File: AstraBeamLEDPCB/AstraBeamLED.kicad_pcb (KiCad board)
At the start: 2 copper layers, 75 x 55 mm, 21 parts

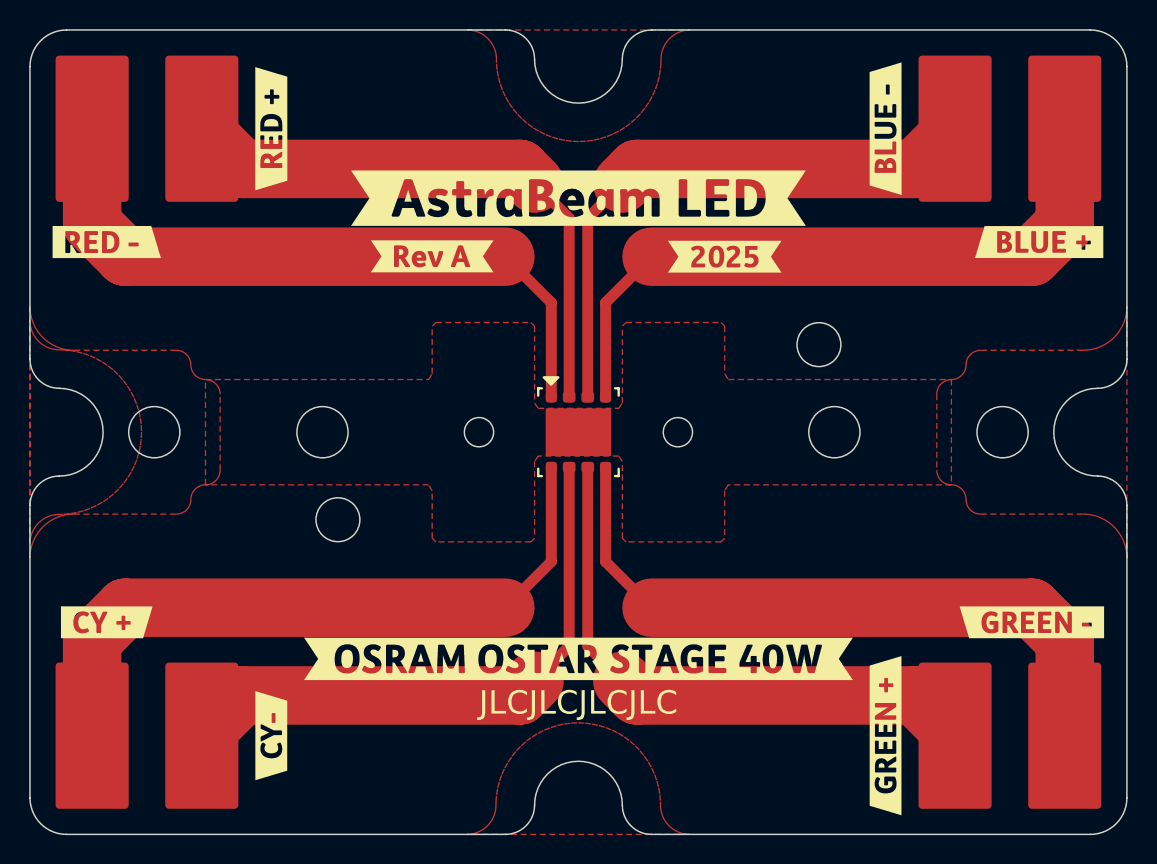
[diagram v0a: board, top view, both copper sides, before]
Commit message: Cleanup copper for production
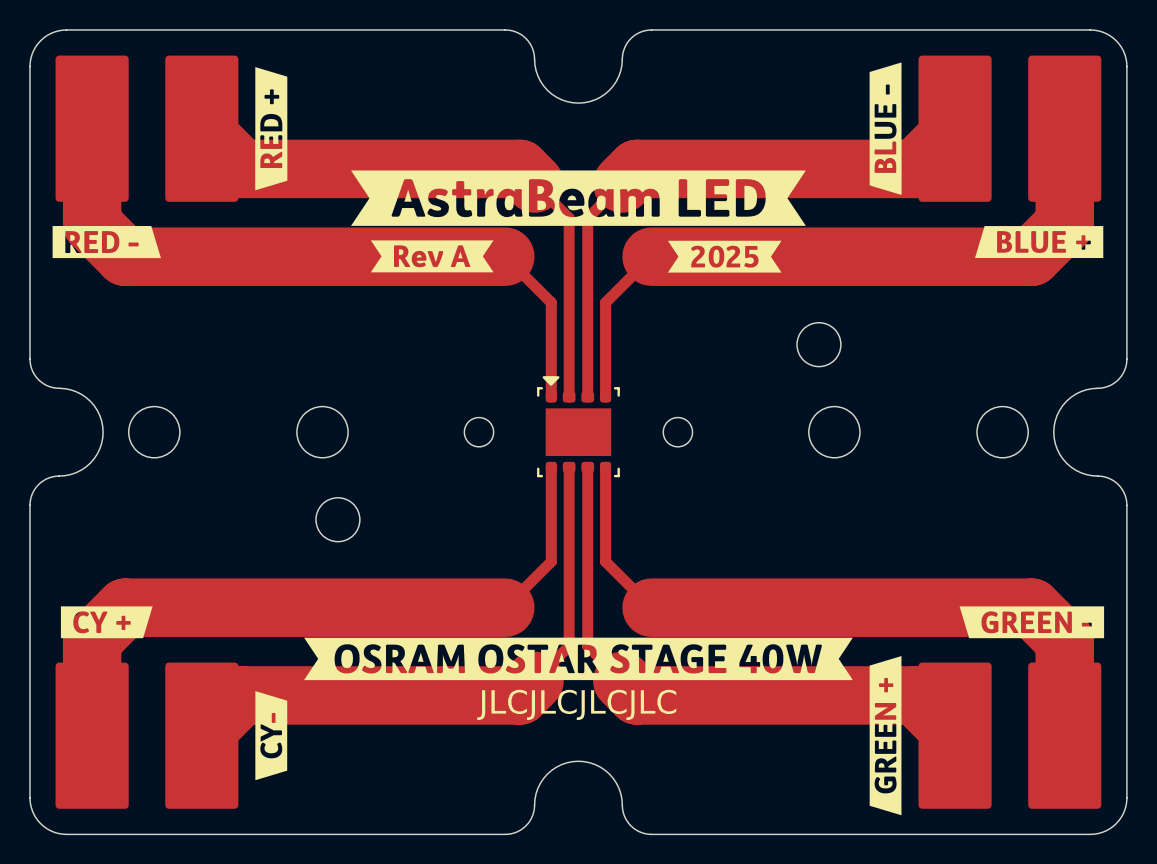
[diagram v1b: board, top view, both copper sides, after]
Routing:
- removed copper zone on F.Cu, net (none)
- removed copper zone on F.Cu, net GND

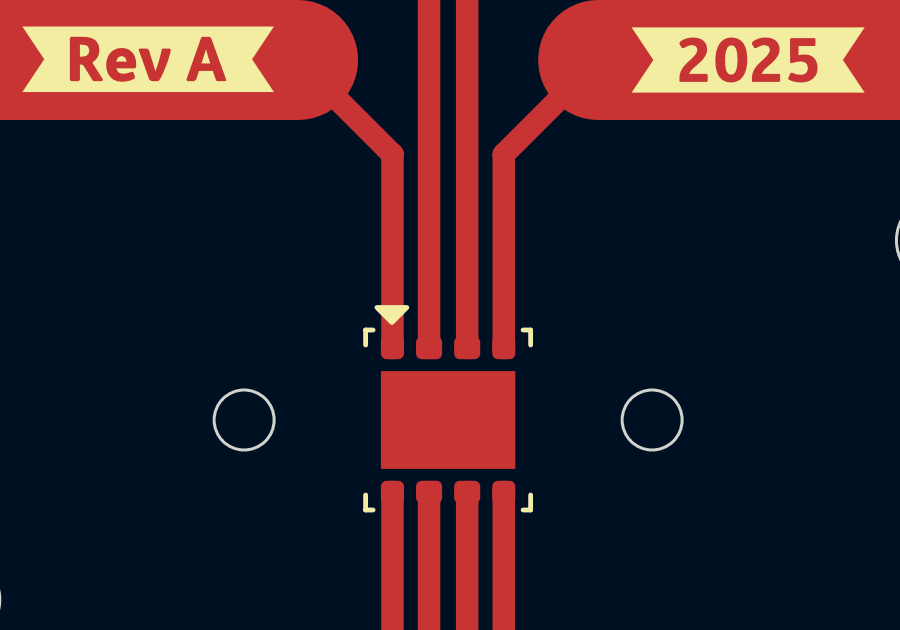
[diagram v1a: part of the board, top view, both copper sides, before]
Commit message: Fix reversed pins
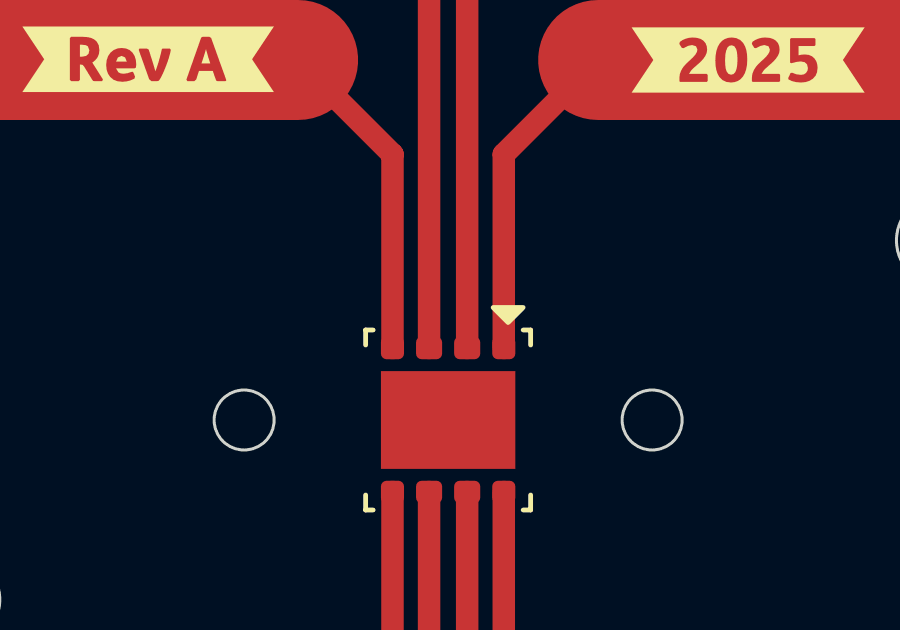
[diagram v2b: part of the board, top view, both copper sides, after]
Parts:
- moved J2 66.5 mm to (116.8, 79.2)
- moved J4 66.5 mm to (183.2, 120.8)
- moved J5 66.5 mm to (183.2, 79.2)
- moved J7 66.5 mm to (116.8, 120.8)
- moved J1 51.5 mm to (175.8, 79.2)
- moved J3 51.5 mm to (124.2, 120.8)
- moved J6 51.5 mm to (124.2, 79.2)
- moved J8 51.5 mm to (175.8, 120.8)

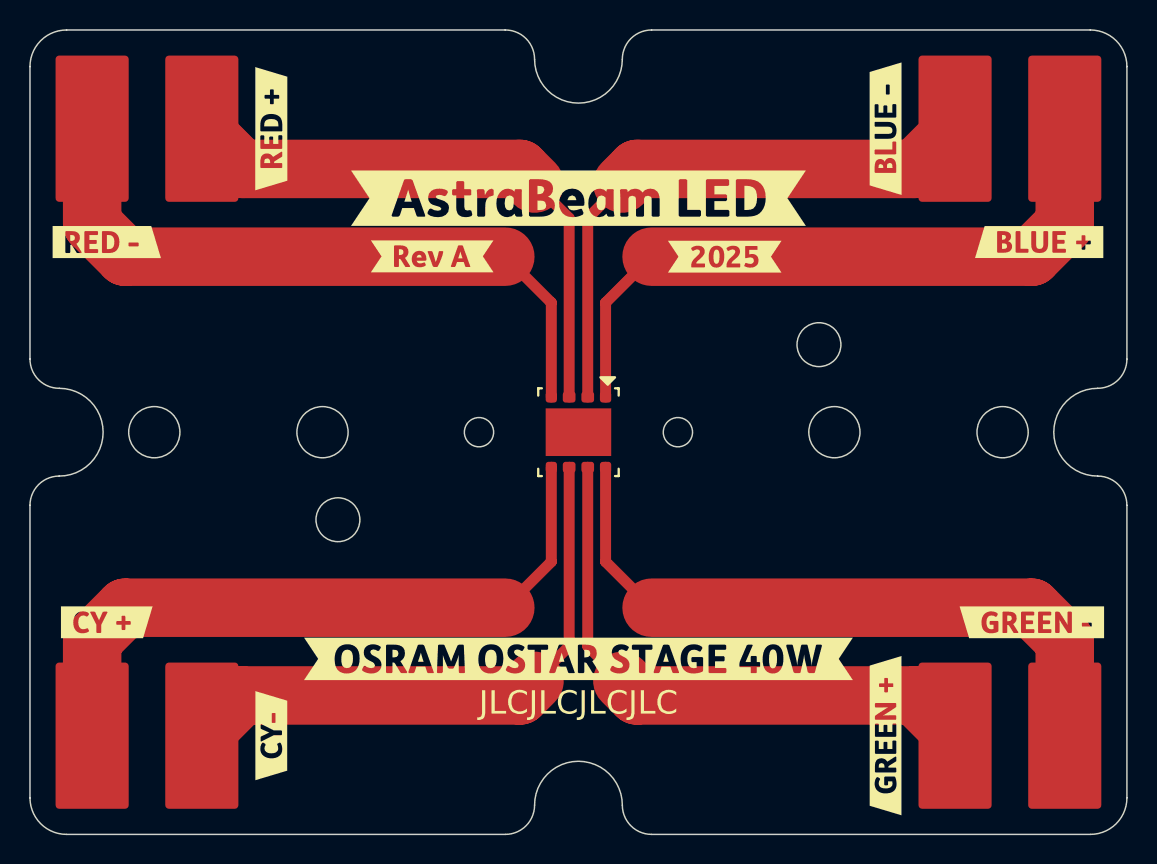
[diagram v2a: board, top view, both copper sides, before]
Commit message: Updated labels, description
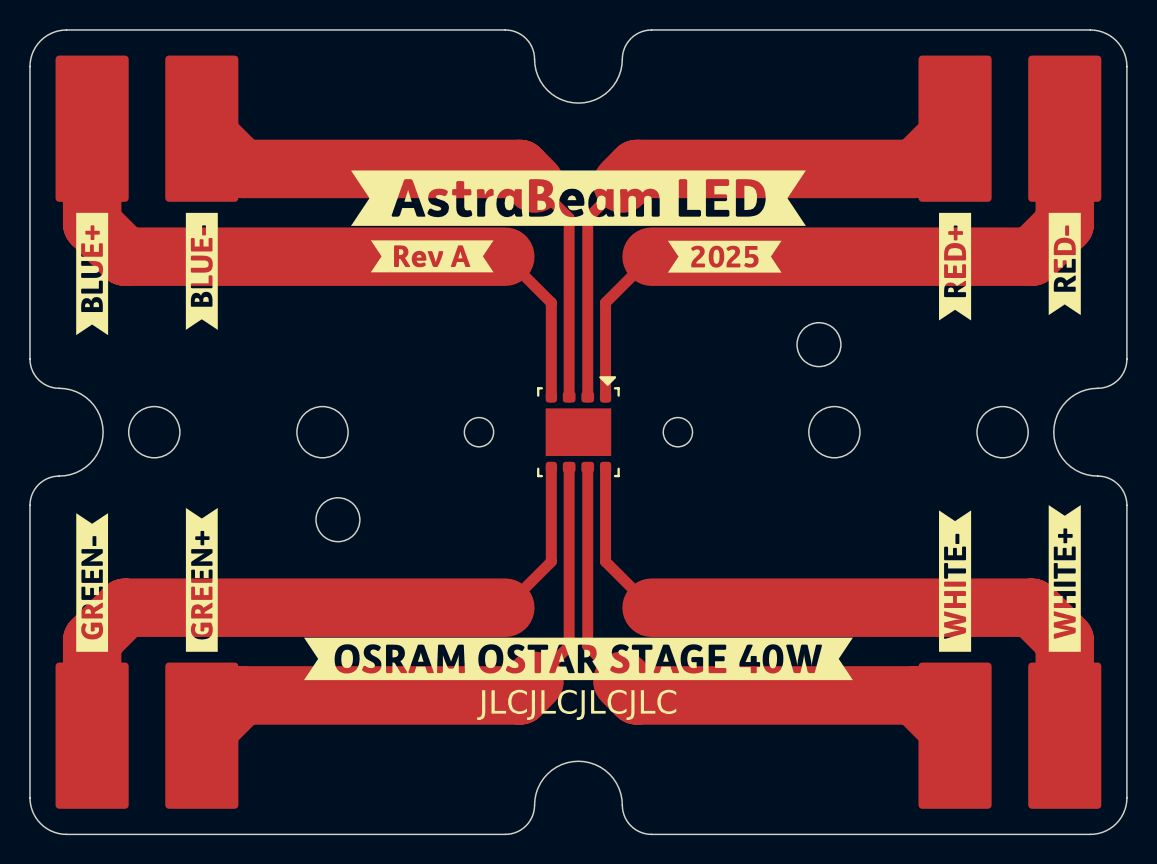
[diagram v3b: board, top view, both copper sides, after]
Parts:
- removed kibuzzard-67294C33: G***, kibuzzard-67294C33
- removed kibuzzard-67294C7C: G***, kibuzzard-67294C7C
- removed kibuzzard-67294CC4: G***, kibuzzard-67294CC4
- removed kibuzzard-67294E62: G***, kibuzzard-67294E62
- removed kibuzzard-67294EA2: G***, kibuzzard-67294EA2
- removed kibuzzard-67294EBF: G***, kibuzzard-67294EBF
- removed kibuzzard-672E94DA: G***, kibuzzard-672E94DA
- removed kibuzzard-672E94E0: G***, kibuzzard-672E94E0
- added kibuzzard-68162CBA: G***, kibuzzard-68162CBA, F.Cu at (183.2, 88.5)
- added kibuzzard-68162CC4: G***, kibuzzard-68162CC4, F.Cu at (175.8, 88.7)
- added kibuzzard-68162CCF: G***, kibuzzard-68162CCF, F.Cu at (124.2, 89.0)
- added kibuzzard-68162CD6: G***, kibuzzard-68162CD6, F.Cu at (116.8, 89.2)
- added kibuzzard-68162D21: G***, kibuzzard-68162D21, F.Cu at (116.8, 110.3)
- added kibuzzard-68162D41: G***, kibuzzard-68162D41, F.Cu at (124.2, 110.1)
- added kibuzzard-68162D54: G***, kibuzzard-68162D54, F.Cu at (175.8, 110.2)
- added kibuzzard-68162D5D: G***, kibuzzard-68162D5D, F.Cu at (183.2, 110.0)
